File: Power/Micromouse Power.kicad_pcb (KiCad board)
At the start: 2 copper layers, 40 parts, among them J1 Battery, J2 Conn_02x08_Odd_Even, U1 AMS1117-3.3, U2 TP4056, U3 DRV8837, U4 DRV8837

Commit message: Initial board layout done
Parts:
- added C10: 10nF, Capacitor_SMD:C_0603_1608Metric, F.Cu at (164.0, 115.6)
- added C11: 100nF, Capacitor_SMD:C_0603_1608Metric, F.Cu at (164.0, 114.1)
- added C12: 10nF, Capacitor_SMD:C_0603_1608Metric, F.Cu at (155.5, 115.6)
- added C13: 100nF, Capacitor_SMD:C_0603_1608Metric, F.Cu at (155.5, 114.1)
- added SW1: SW_SPST, Button_Switch_SMD:Nidec_Copal_CAS-120A, F.Cu at (146.5, 109.0)
- TP1, TP10, TP2, TP3, TP8, TP9: moved to B.Cu
- moved TP5 101.5 mm to (156.9, 118.0)
- moved TP4 98.0 mm to (161.2, 120.3)
- moved C7 93.2 mm to (152.4, 115.6)
- moved C8 92.3 mm to (152.4, 114.1)
- moved TP10 91.9 mm to (154.2, 120.6), turned to 180 degrees
- moved U4 91.7 mm to (154.0, 117.7)
- moved TP9 91.1 mm to (153.3, 115.7), turned to 180 degrees
- moved U3 88.7 mm to (162.4, 117.7)
- moved C4 87.1 mm to (160.9, 114.1), turned to 0 degrees
- moved C5 86.3 mm to (160.9, 115.6), turned to 0 degrees
- moved TP7 85.6 mm to (165.6, 117.3)
- moved TP2 81.5 mm to (162.2, 124.8), turned to 180 degrees
- moved TP1 81.4 mm to (162.8, 116.0), turned to 180 degrees
- moved TP6 81.4 mm to (172.0, 120.5)
- moved JP3 78.1 mm to (165.7, 120.5), turned to 90 degrees
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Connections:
- U3 pad 5: /PC7 -> /PC6
- U3 pad 6: /PC6 -> /PC7
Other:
- board outline added: 37.5 x 22.4 mm

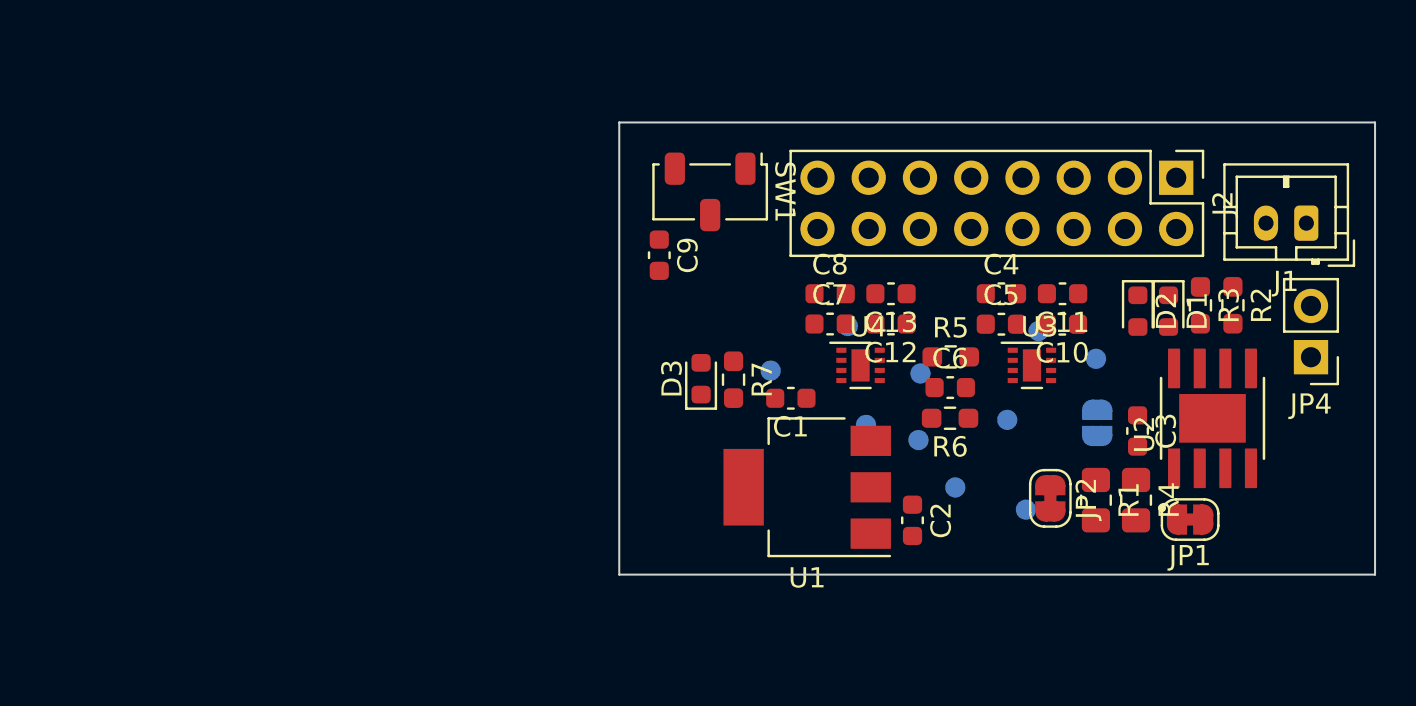
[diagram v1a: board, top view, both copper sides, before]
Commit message: Added switch circuit
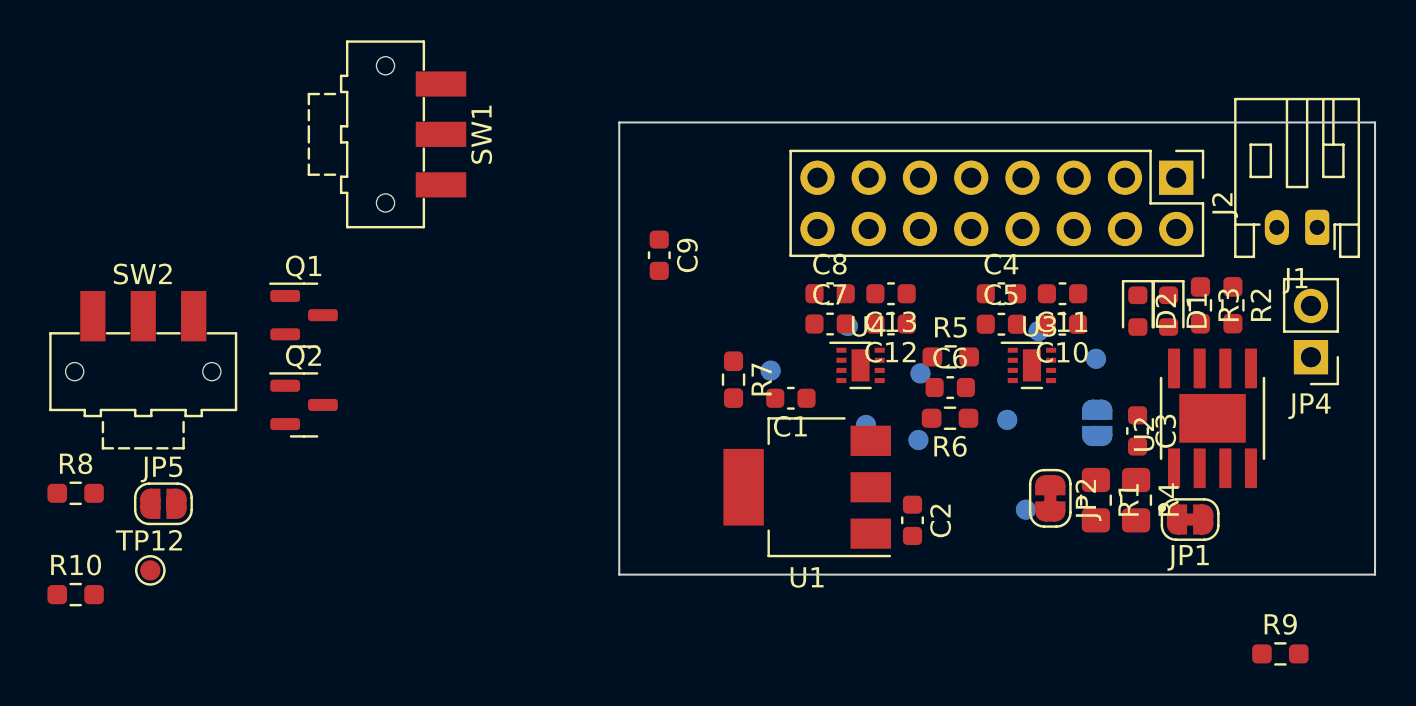
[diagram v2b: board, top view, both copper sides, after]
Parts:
- removed D3: green, LED_SMD:LED_0603_1608Metric
- removed TP11: Batt, TestPoint:TestPoint_Pad_D1.0mm
- added JP5: Batt_Switch, Jumper:SolderJumper-2_P1.3mm_Open_RoundedPad1.0x1.5mm, F.Cu at (119.4, 124.5)
- added Q1: AO3401A, Package_TO_SOT_SMD:SOT-23, F.Cu at (126.4, 115.2)
- added Q2: AO3401A, Package_TO_SOT_SMD:SOT-23, F.Cu at (126.4, 119.6)
- added R10: 0R, Resistor_SMD:R_0603_1608Metric_Pad0.98x0.95mm_HandSolder, F.Cu at (115.1, 129.0)
- added R8: 10k, Resistor_SMD:R_0603_1608Metric_Pad0.98x0.95mm_HandSolder, F.Cu at (115.1, 124.0)
- added R9: 0R, Resistor_SMD:R_0603_1608Metric_Pad0.98x0.95mm_HandSolder, F.Cu at (174.8, 131.9)
- added SW2: pwr, Button_Switch_SMD:SW_SPDT_CK-JS102011SAQN, F.Cu at (118.4, 118.0)
- added TP12: Batt_Sw, TestPoint:TestPoint_Pad_D1.0mm, F.Cu at (118.8, 127.8)
- J1: footprint Connector_JST:JST_PH_B2B-PH-K_1x02_P2.00mm_Vertical -> Connector_JST:JST_PH_S2B-PH-K_1x02_P2.00mm_Horizontal
- R7: value 1k -> 10k
- SW1: value SW_SPST -> pwr; footprint Button_Switch_SMD:Nidec_Copal_CAS-120A -> Button_Switch_SMD:SW_SPDT_CK-JS102011SAQN
- moved SW1 16.3 mm to (130.4, 106.2)
- moved J1 0.58 mm to (176.6, 110.8)
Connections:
- C1 pad 1: BATT_SWITCHED -> BATT
- J2 pad 7: +BATT -> BATT
- J2 pad 8: +BATT -> BATT
- JP4 pad 2: +BATT -> BATT
- R7 pad 1: Net-(D3-A) -> +BATT
- R7 pad 2: +3V3 -> Net-(Q1-G)
- SW1 pad 1: +BATT -> unconnected-(SW1-A-Pad1)
- SW1 pad 2: BATT_SWITCHED -> GND
- SW1 pad 3: (no net) -> Net-(Q1-G)
- U1 pad 3: BATT_SWITCHED -> BATT

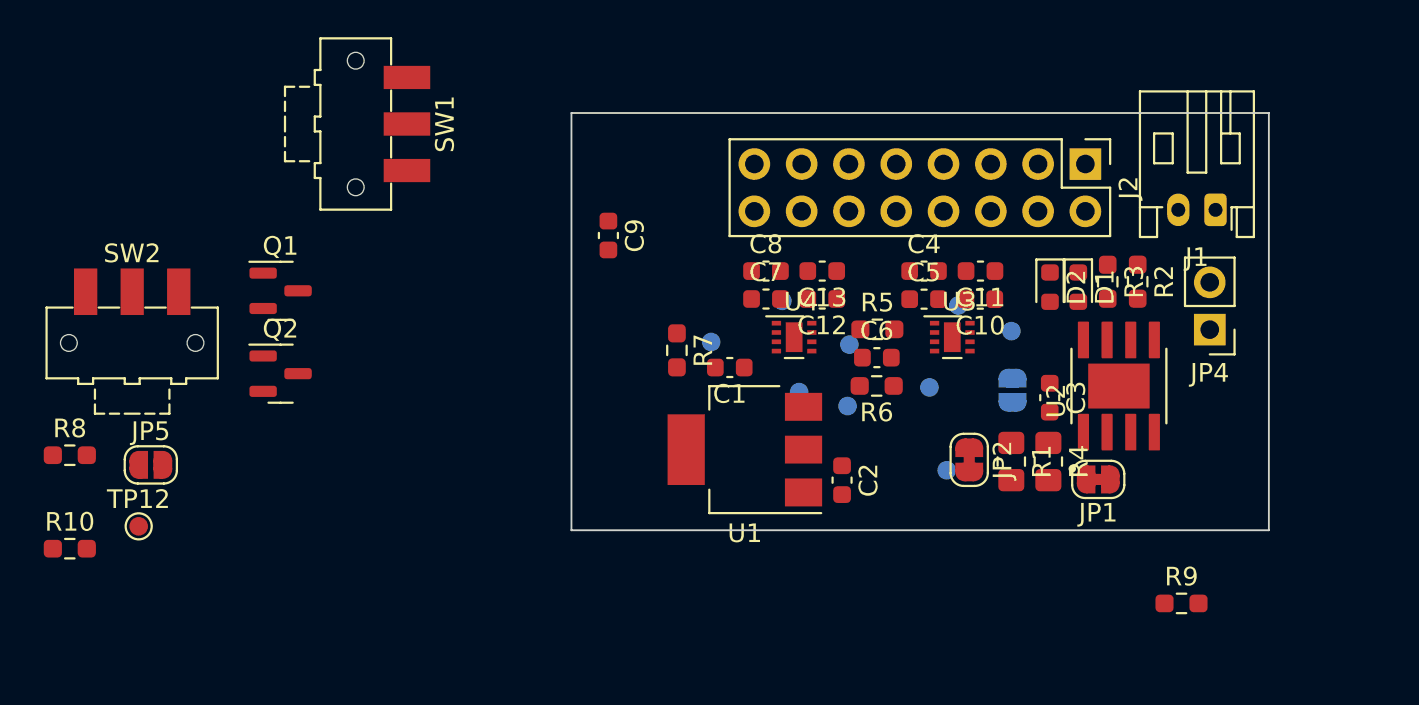
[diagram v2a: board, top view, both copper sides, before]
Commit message: Routing and removes power decoup
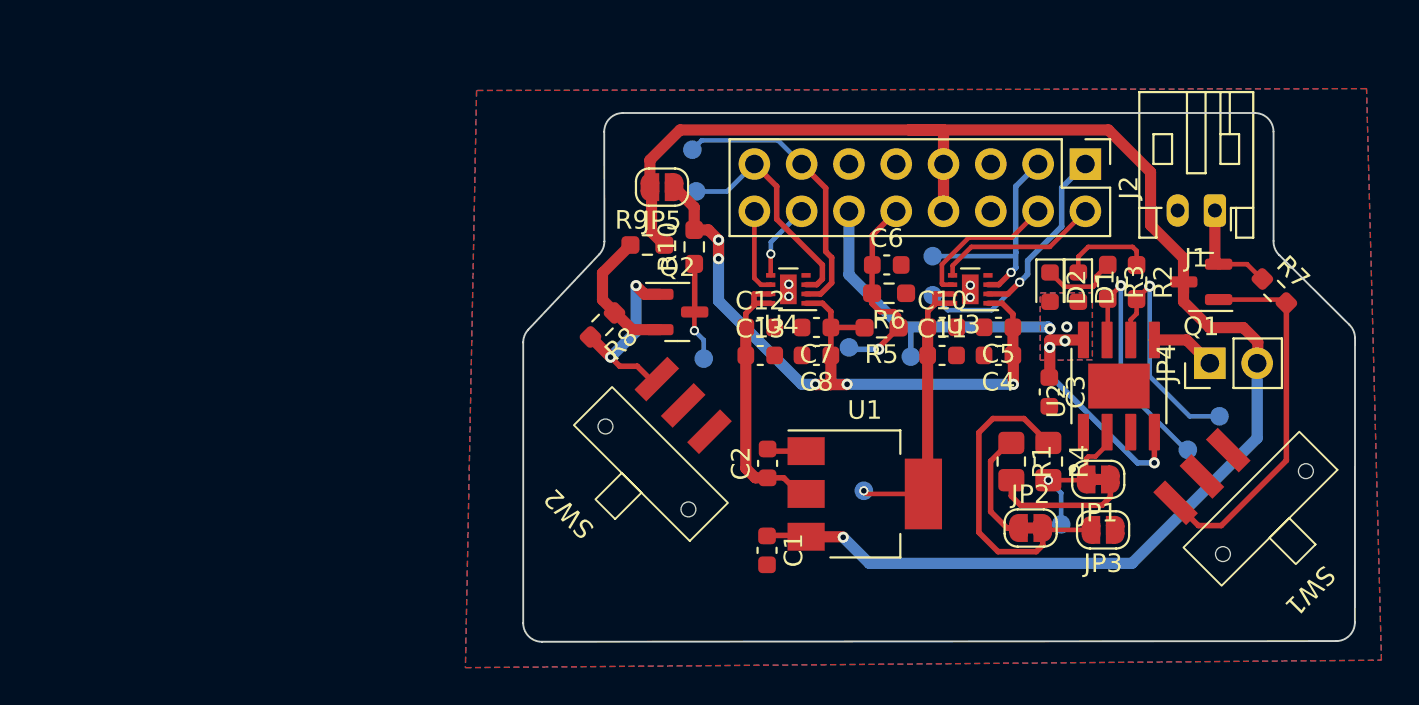
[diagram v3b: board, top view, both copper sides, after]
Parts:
- removed C9: 10uF, Capacitor_SMD:C_0603_1608Metric
- JP3: moved to F.Cu
- SW1, SW2: footprint Button_Switch_SMD:SW_SPDT_CK-JS102011SAQN -> MyLibrary:SMD_SPDT
- TP12: moved to B.Cu
- moved SW1 56.1 mm to (180.1, 132.2), turned to -135 degrees
- moved Q1 49.4 mm to (175.8, 114.7), turned to 180 degrees
- moved R10 37.2 mm to (148.6, 112.8), turned to 90 degrees
- moved R9 34.5 mm to (146.1, 112.7), turned to 180 degrees
- moved R7 32.2 mm to (179.8, 115.2), turned to -45 degrees
- moved TP12 31.7 mm to (149.1, 118.8), turned to 180 degrees
- moved JP5 31.2 mm to (146.9, 109.6), turned to 180 degrees
- moved R8 29.5 mm to (143.7, 117.0), turned to -135 degrees
- moved TP6 26.8 mm to (148.5, 107.6)
- moved SW2 23.8 mm to (140.9, 125.6), turned to 135 degrees
- moved Q2 21.6 mm to (147.7, 116.3)
- moved TP7 18.5 mm to (148.7, 109.8)
- moved TP1 15.2 mm to (176.8, 121.9)
- moved TP3 13.1 mm to (168.3, 127.7)
- moved TP2 13.0 mm to (175.1, 123.7)
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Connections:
- TP4 pad 1: /Motor1_A -> /Motor2_A
- TP5 pad 1: /Motor1_B -> /Motor2_B
- TP6 pad 1: /Motor2_A -> /Motor1_A
- TP7 pad 1: /Motor2_B -> /Motor1_B
- U3 pad 2: /Motor1_A -> /Motor2_A
- U3 pad 3: /Motor1_B -> /Motor2_B
- U4 pad 2: /Motor2_A -> /Motor1_A
- U4 pad 3: /Motor2_B -> /Motor1_B
- U4 pad 5: /PC9 -> /PC8
- U4 pad 6: /PC8 -> /PC9
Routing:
- net BATT: track 0.00 -> 87.7 mm, vias 0 -> 1
- net BATT_SWITCHED: track 0.00 -> 40.7 mm, vias 0 -> 5
- net +3V3: track 0.00 -> 31.9 mm, vias 0 -> 1
- net +5V: track 0.00 -> 31.7 mm, vias 0 -> 5
- net Net-(Q1-G): track 0.00 -> 19.9 mm
- net Net-(JP2-B): track 0.00 -> 17.2 mm
- net /Motor2_A: track 0.00 -> 15.5 mm, vias 0 -> 1
- net /Motor1_A: track 0.00 -> 15.3 mm
- net Net-(U2-~{CHRG}): track 0.00 -> 13.6 mm, vias 0 -> 1
- net Net-(U2-~{STDBY}): track 0.00 -> 12.7 mm, vias 0 -> 1
- net /Motor1_B: track 0.00 -> 12.6 mm
- net /Motor2_B: track 0.00 -> 12.4 mm, vias 0 -> 1
- net /BATT_ADC: track 0.08 -> 11.2 mm, vias 0 -> 1
- net Net-(Q2-G): track 0.00 -> 10.4 mm, vias 0 -> 2
- net /PC6: track 0.00 -> 8.86 mm
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- added copper zone on B.Cu, net +5V
- added copper zone on F.Cu, net +5V
- added copper zone on B.Cu, net GND
- added copper zone on F.Cu, net GND
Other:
- board size 37.5 x 22.4 mm -> 44.7 x 28.4 mm

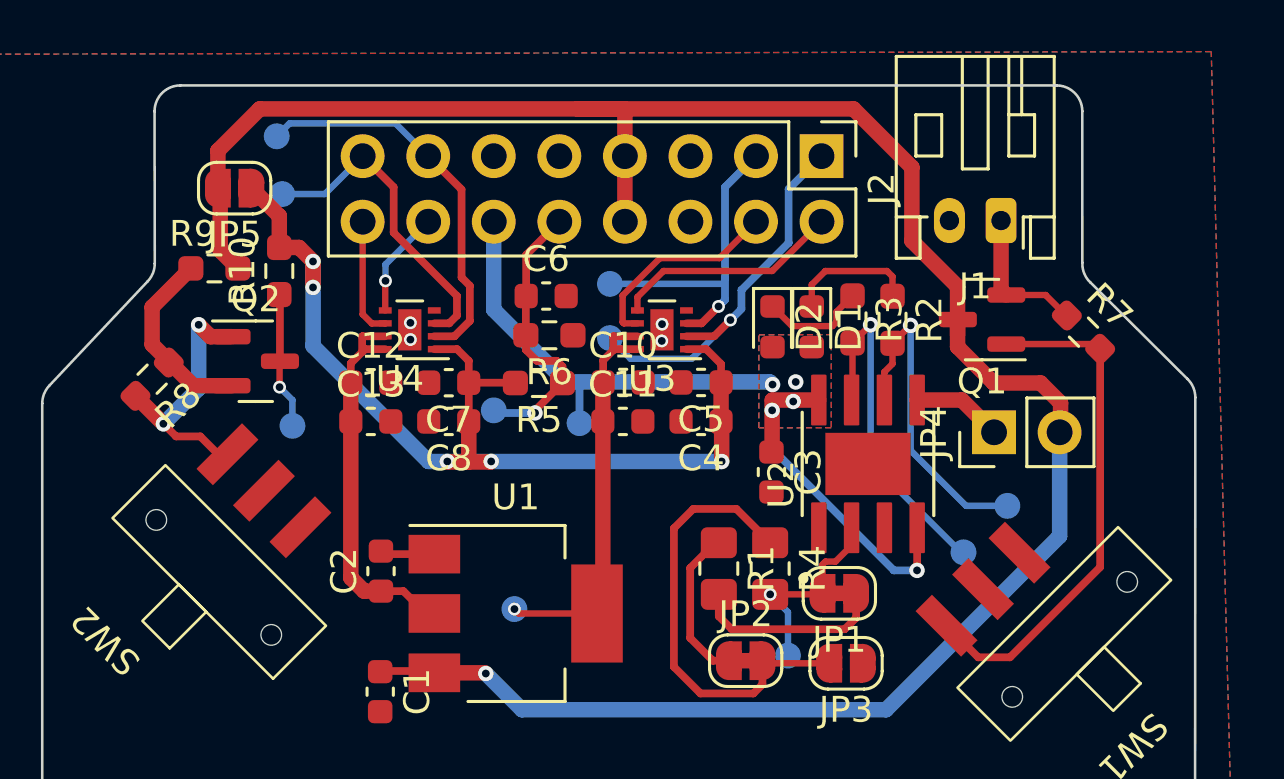
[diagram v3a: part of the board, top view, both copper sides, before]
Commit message: Updated routing
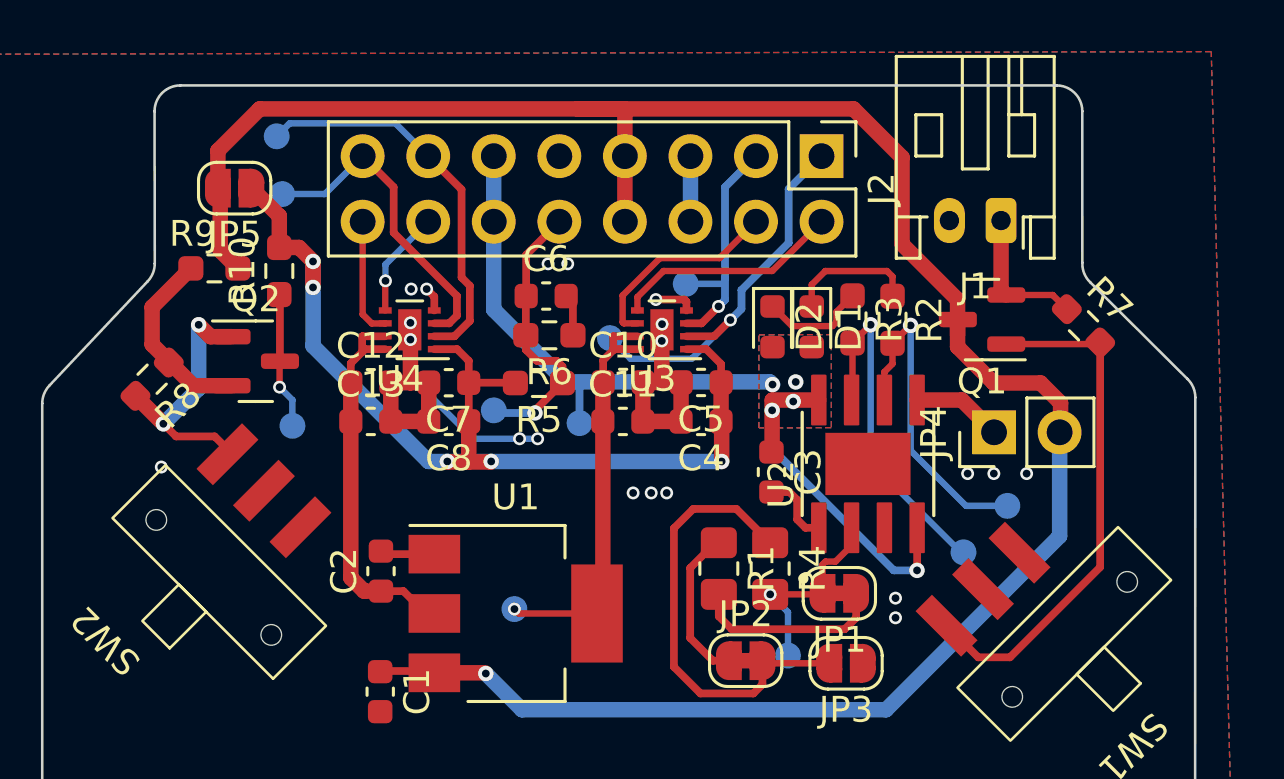
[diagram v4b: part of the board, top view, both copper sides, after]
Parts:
- moved TP5 2.94 mm to (164.3, 113.3)
- moved R7 0.25 mm to (179.8, 114.9)
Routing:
- net GND: track 2.12 -> 34.4 mm, vias 4 -> 20
- net /Motor2_B: track 12.4 -> 9.46 mm
- net +5V: track 31.7 -> 34.2 mm

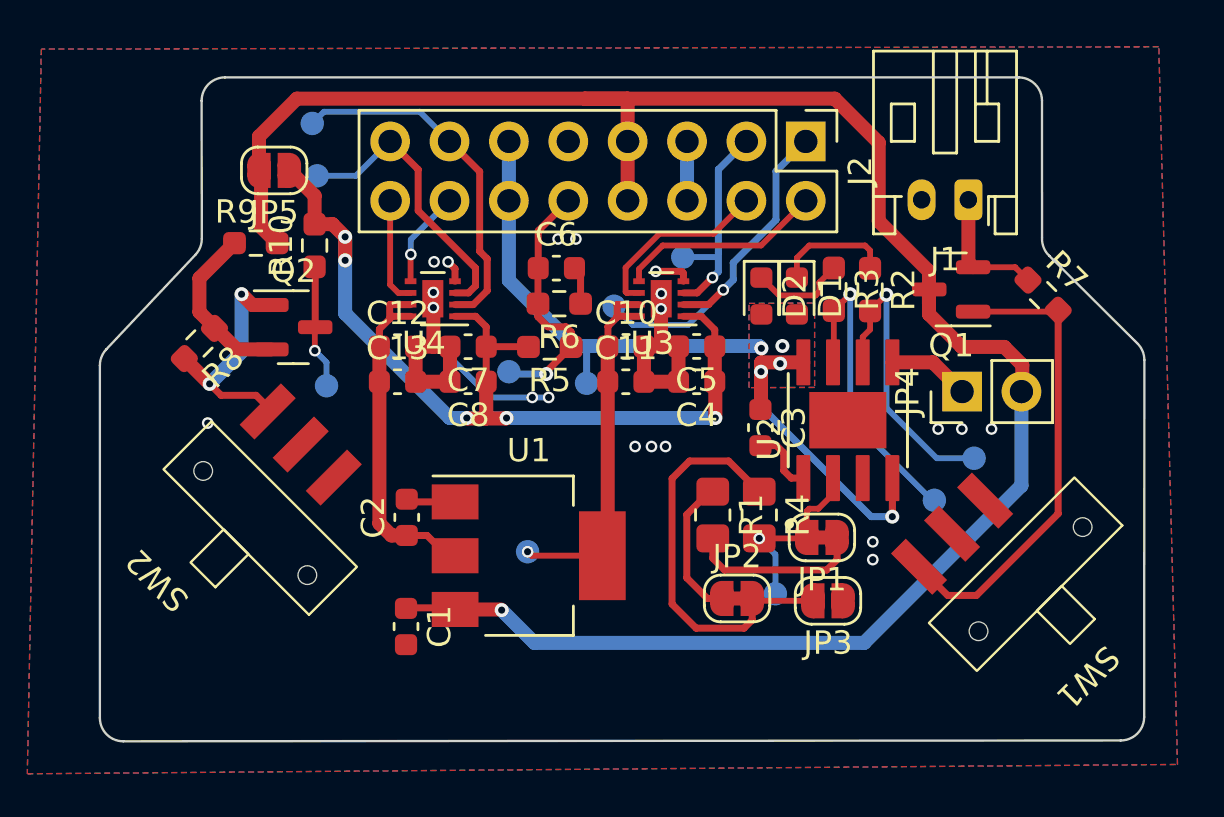
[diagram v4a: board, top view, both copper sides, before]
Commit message: Updated document titles
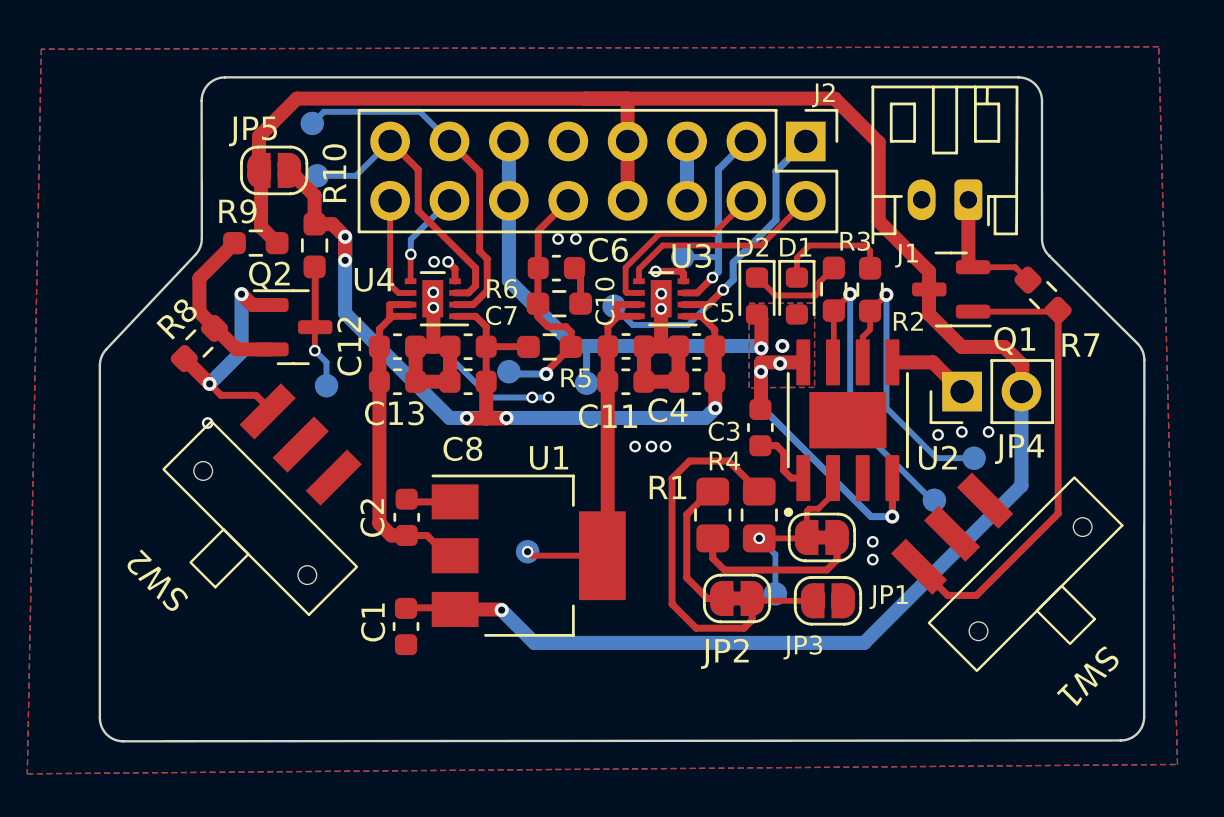
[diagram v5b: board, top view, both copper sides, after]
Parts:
- moved D2 0.19 mm to (167.5, 115.0)
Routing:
- net +5V: track 34.2 -> 35.7 mm
